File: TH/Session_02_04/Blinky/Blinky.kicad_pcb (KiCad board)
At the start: 2 copper layers, 38.1 x 38.1 mm, 12 parts, among them U1 TLC551CD‎

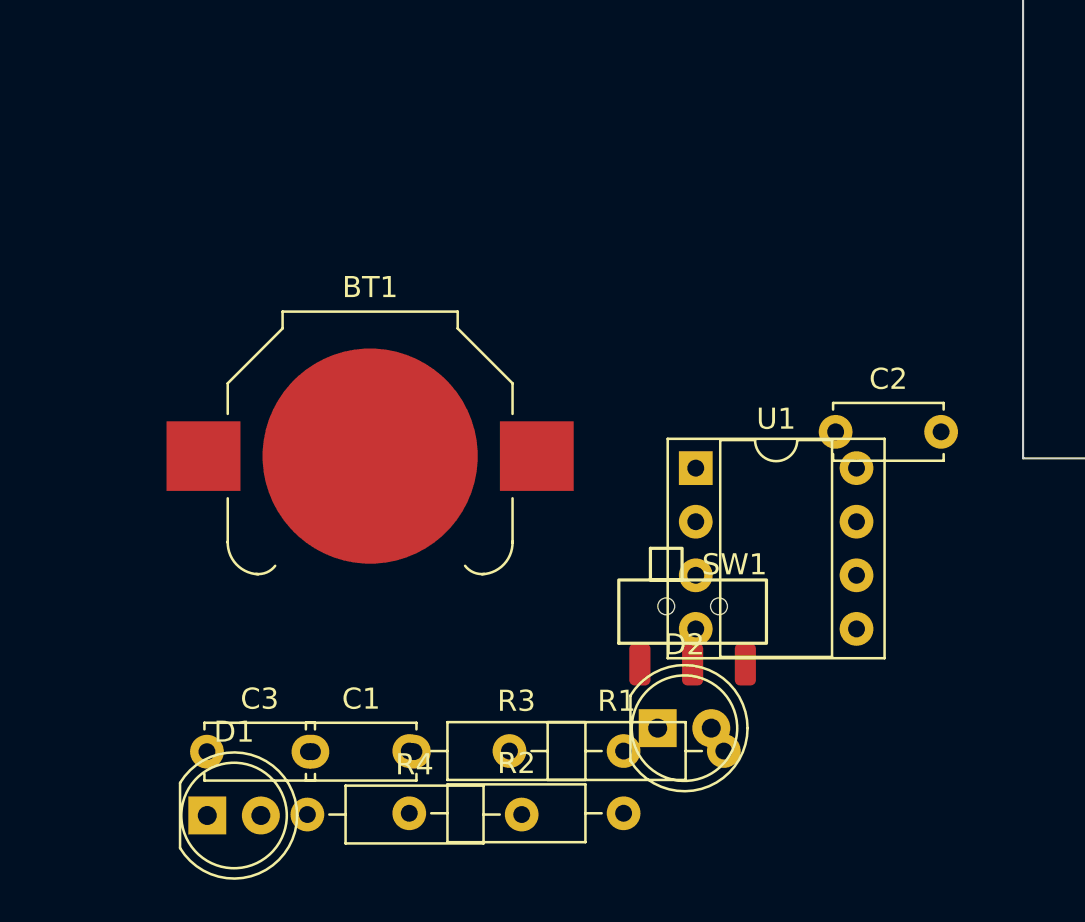
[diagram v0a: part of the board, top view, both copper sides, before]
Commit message: Revamps the through-hole project as transistor based
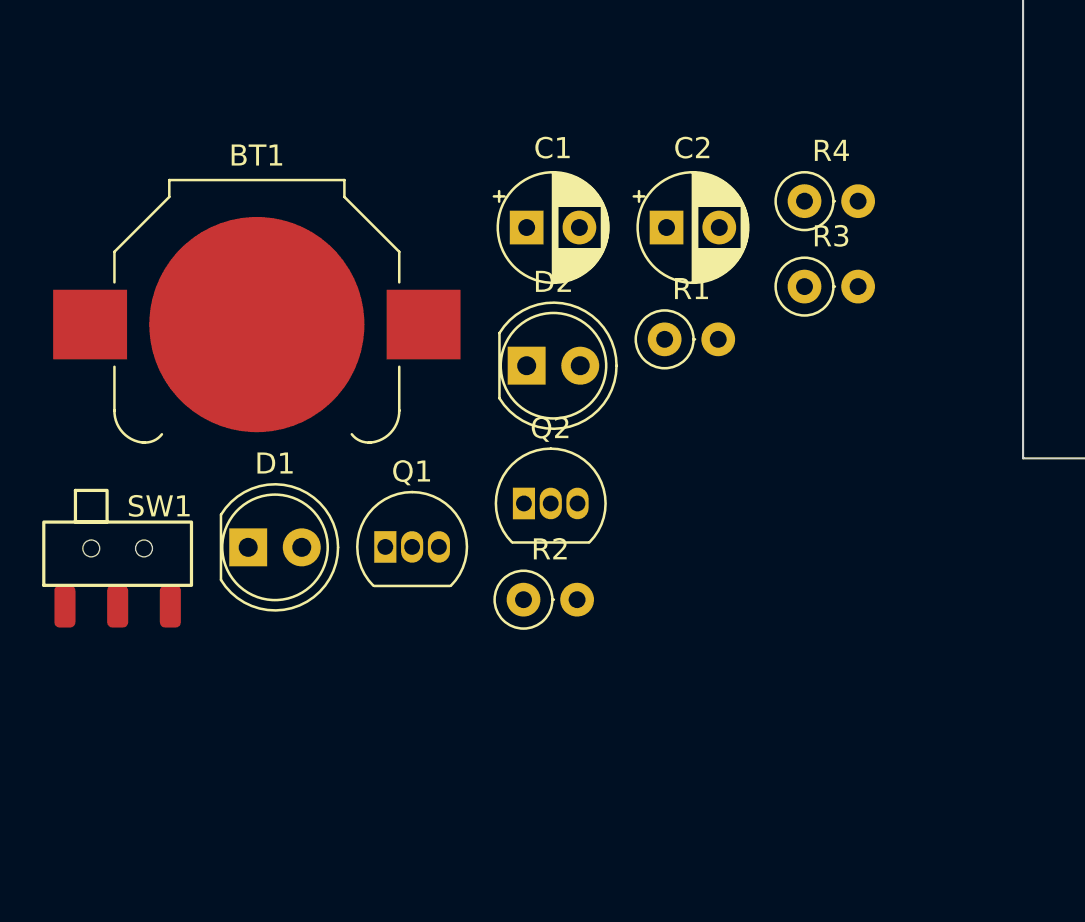
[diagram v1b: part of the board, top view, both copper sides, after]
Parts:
- removed C3: 100nF, Capacitor_THT:C_Disc_D5.0mm_W2.5mm_P5.00mm
- removed SW?: SW_SPDT, Blinky_ZAM:SSK-1202
- removed U1: TLC551CD‎, Package_DIP:DIP-8_W7.62mm_Socket
- added Q1: 2N3904, Package_TO_SOT_THT:TO-92_Inline, F.Cu at (142.0, 95.0)
- added Q2: 2N3904, Package_TO_SOT_THT:TO-92_Inline, F.Cu at (148.5, 92.9)
- added SW1: SW_SPST, Blinky_ZAM:SSK-1202, F.Cu at (129.3, 97.8)
- C1: value 300nF -> 10μF; footprint Capacitor_THT:C_Disc_D5.0mm_W2.5mm_P5.00mm -> Capacitor_THT:CP_Radial_D5.0mm_P2.50mm
- C2: value 100nF -> 10μF; footprint Capacitor_THT:C_Disc_D5.0mm_W2.5mm_P5.00mm -> Capacitor_THT:CP_Radial_D5.0mm_P2.50mm
- R1: value 10kΩ -> 220Ω; footprint Resistor_THT:R_Axial_DIN0207_L6.3mm_D2.5mm_P10.16mm_Horizontal -> Resistor_THT:R_Axial_DIN0207_L6.3mm_D2.5mm_P2.54mm_Vertical
- R2: value 1MΩ -> 100kΩ; footprint Resistor_THT:R_Axial_DIN0207_L6.3mm_D2.5mm_P10.16mm_Horizontal -> Resistor_THT:R_Axial_DIN0207_L6.3mm_D2.5mm_P2.54mm_Vertical
- R3: value 200Ω -> 100kΩ; footprint Resistor_THT:R_Axial_DIN0207_L6.3mm_D2.5mm_P10.16mm_Horizontal -> Resistor_THT:R_Axial_DIN0207_L6.3mm_D2.5mm_P2.54mm_Vertical
- R4: value 200Ω -> 220Ω; footprint Resistor_THT:R_Axial_DIN0207_L6.3mm_D2.5mm_P10.16mm_Horizontal -> Resistor_THT:R_Axial_DIN0207_L6.3mm_D2.5mm_P2.54mm_Vertical
- moved R4 37.4 mm to (161.8, 78.6)
- moved R3 28.9 mm to (161.8, 82.6)
- moved C1 26.9 mm to (148.7, 79.8)
- moved R1 20.9 mm to (155.2, 85.1)
- moved D2 18.3 mm to (148.7, 86.4)
- moved D1 12.9 mm to (135.5, 95.0)
- moved C2 12.6 mm to (155.3, 79.8)
- moved R2 11.5 mm to (148.5, 97.5)
- moved BT1 8.23 mm to (135.9, 84.4)
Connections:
- C1 pad 2: GND -> Net-(C1-Pad2)
- C2 pad 2: GND -> Net-(C2-Pad2)
- D1 pad 1: Net-(D1-Pad1) -> Net-(C1-Pad2)
- D1 pad 2: Net-(C2-Pad1) -> Net-(D1-Pad2)
- D2 pad 1: Net-(D2-Pad1) -> Net-(C2-Pad2)
- R1 pad 1: Net-(C2-Pad1) -> Net-(R1-Pad1)
- R1 pad 2: Net-(R1-Pad2) -> Net-(D1-Pad2)
- R2 pad 1: Net-(R1-Pad2) -> Net-(R1-Pad1)
- R3 pad 1: Net-(D1-Pad1) -> Net-(R1-Pad1)
- R3 pad 2: Net-(D2-Pad2) -> Net-(C2-Pad1)
- R4 pad 1: Net-(D2-Pad1) -> Net-(R1-Pad1)
- R4 pad 2: GND -> Net-(D2-Pad2)

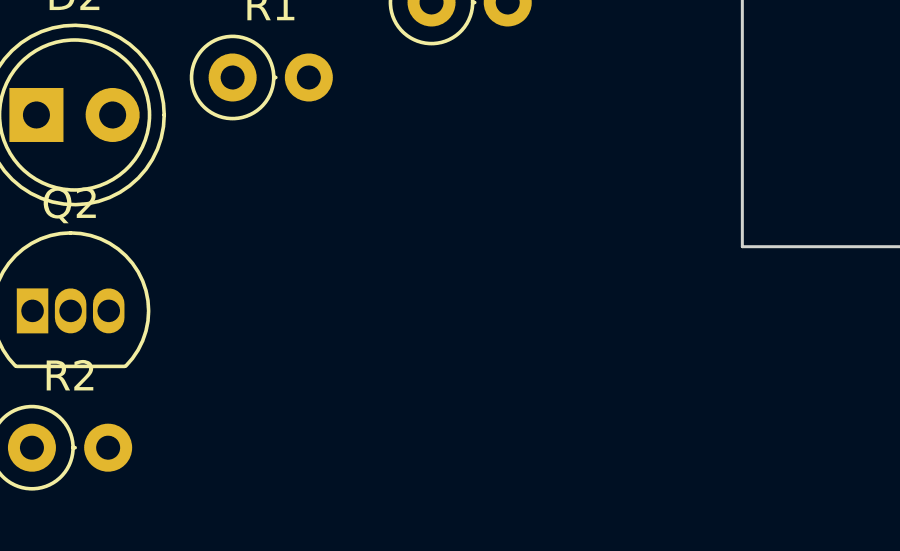
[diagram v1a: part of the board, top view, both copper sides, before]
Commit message: Makes corrections to the design rules
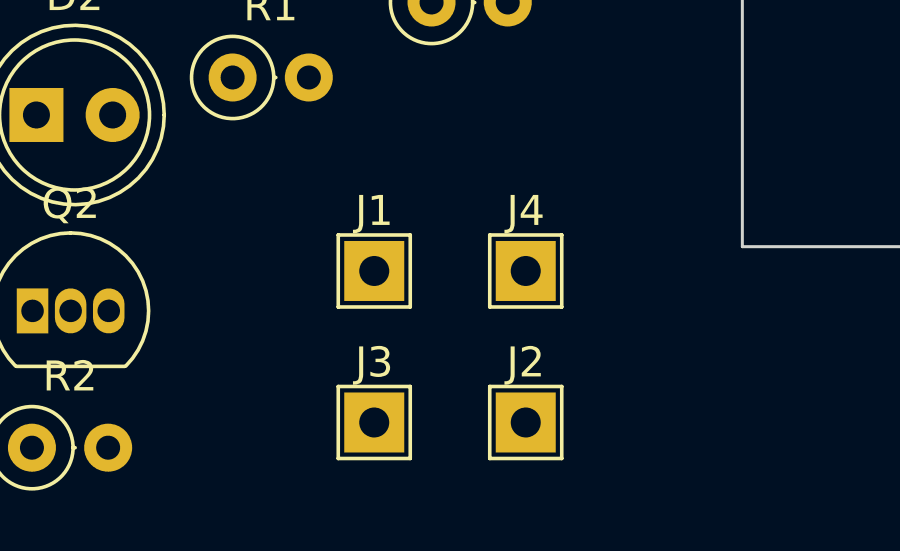
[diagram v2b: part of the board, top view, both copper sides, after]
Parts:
- added J1: Jumper_1, TestPoint:TestPoint_THTPad_2.0x2.0mm_Drill1.0mm, F.Cu at (159.9, 91.6)
- added J2: Jumper_1, TestPoint:TestPoint_THTPad_2.0x2.0mm_Drill1.0mm, F.Cu at (165.0, 96.6)
- added J4: Jumper_1, TestPoint:TestPoint_THTPad_2.0x2.0mm_Drill1.0mm, F.Cu at (165.0, 91.6)
- added J?: Jumper_1, TestPoint:TestPoint_THTPad_2.0x2.0mm_Drill1.0mm, F.Cu at (159.9, 96.6)
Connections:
- Q1 pad 2: Net-(C2-Pad1) -> Net-(J1-Pad1)
- Q2 pad 2: Net-(C1-Pad1) -> Net-(J4-Pad1)
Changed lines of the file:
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@@
     (48 "B.Fab" user)
     (49 "F.Fab" user)
-    (50 "User.1" user)
-    (51 "User.2" user)
-    (52 "User.3" user)
-    (53 "User.4" user)
-    (54 "User.5" user)
-    (55 "User.6" user)
-    (56 "User.7" user)
-    (57 "User.8" user)
-    (58 "User.9" user)
+    (50 "User.1" user "Nutzer.1")
+    (51 "User.2" user "Nutzer.2")
+    (52 "User.3" user "Nutzer.3")
+    (53 "User.4" user "Nutzer.4")
+    (54 "User.5" user "Nutzer.5")
+    (55 "User.6" user "Nutzer.6")
+    (56 "User.7" user "Nutzer.7")
+    (57 "User.8" user "Nutzer.8")
+    (58 "User.9" user "Nutzer.9")
   )
   (setup
@@
   (net 8 "Net-(D2-Pad2)")
   (net 9 "Net-(R1-Pad1)")
+  (net 10 "Net-(J1-Pad1)")
+  (net 11 "Net-(J4-Pad1)")
   (footprint "LED_THT:LED_D5.0mm" (layer "F.Cu")
     (at 135.459775 94.98)
@@
     )
   )
+  (footprint "TestPoint:TestPoint_THTPad_2.0x2.0mm_Drill1.0mm" (layer "F.Cu")
+    (at 159.92 96.62)
+    (descr "THT rectangular pad as test Point, square 2.0mm_Drill1.0mm  side length, hole diameter 1.0mm")
+    (tags "test point THT pad rectangle square")
+    (property "Reference" "J?")
+    (property "Sheetfile" "Blinky.kicad_sch")
+    (property "Sheetname" "")
+    (property "Value" "Jumper_1")
+    (attr exclude_from_pos_files)
+    (fp_text reference "J3" (at 0 -1.998) (layer "F.SilkS")
+      (effects (font (size 1 1) (thickness 0.15)))
+    )
+    (fp_text value "Jumper_1" (at 0 2.05) (layer "F.Fab")
+      (effects (font (size 1 1) (thickness 0.15)))
+    )
+    (fp_text user "${REFERENCE}" (at 0 -2) (layer "F.Fab")
+      (effects (font (size 1 1) (thickness 0.15)))
+    )
+    (fp_line (start 1.2 1.2) (end -1.2 1.2) (layer "F.SilkS") (width 0.12))
+    (fp_line (start -1.2 -1.2) (end 1.2 -1.2) (layer "F.SilkS") (width 0.12))
+    (fp_line (start 1.2 -1.2) (end 1.2 1.2) (layer "F.SilkS") (width 0.12))
+    (fp_line (start -1.2 1.2) (end -1.2 -1.2) (layer "F.SilkS") (width 0.12))
+    (fp_line (start 1.5 1.5) (end 1.5 -1.5) (layer "F.CrtYd") (width 0.05))
+    (fp_line (start -1.5 -1.5) (end -1.5 1.5) (layer "F.CrtYd") (width 0.05))
+    (fp_line (start -1.5 -1.5) (end 1.5 -1.5) (layer "F.CrtYd") (width 0.05))
+    (fp_line (start 1.5 1.5) (end -1.5 1.5) (layer "F.CrtYd") (width 0.05))
+    (pad "1" thru_hole rect (at 0 0) (size 2 2) (drill 1) (layers *.Cu *.Mask)
+      (net 4 "Net-(C2-Pad1)") (pintype "unspecified"))
+  )
   (footprint "Package_TO_SOT_THT:TO-92_Inline" (layer "F.Cu")
     (at 141.96 94.96)
@@
       (net 2 "GND") (pinfunction "E") (pintype "passive"))
     (pad "2" thru_hole oval (at 1.27 0) (size 1.05 1.5) (drill 0.75) (layers *.Cu *.Mask)
-      (net 4 "Net-(C2-Pad1)") (pinfunction "B") (pintype "passive"))
+      (net 10 "Net-(J1-Pad1)") (pinfunction "B") (pintype "passive"))
     (pad "3" thru_hole oval (at 2.54 0) (size 1.05 1.5) (drill 0.75) (layers *.Cu *.Mask)
       (net 5 "Net-(C1-Pad2)") (pinfunction "C") (pintype "passive"))
@@
       (net 2 "GND") (pinfunction "E") (pintype "passive"))
     (pad "2" thru_hole oval (at 1.27 0) (size 1.05 1.5) (drill 0.75) (layers *.Cu *.Mask)
-      (net 3 "Net-(C1-Pad1)") (pinfunction "B") (pintype "passive"))
+      (net 11 "Net-(J4-Pad1)") (pinfunction "B") (pintype "passive"))
     (pad "3" thru_hole oval (at 2.54 0) (size 1.05 1.5) (drill 0.75) (layers *.Cu *.Mask)
       (net 6 "Net-(C2-Pad2)") (pinfunction "C") (pintype "passive"))
@@
       (rotate (xyz 0 0 0))
     )
+  )
+  (footprint "TestPoint:TestPoint_THTPad_2.0x2.0mm_Drill1.0mm" (layer "F.Cu")
+    (at 164.97 91.57)
+    (descr "THT rectangular pad as test Point, square 2.0mm_Drill1.0mm  side length, hole diameter 1.0mm")
+    (tags "test point THT pad rectangle square")
+    (property "Sheetfile" "Blinky.kicad_sch")
+    (property "Sheetname" "")
+    (attr exclude_from_pos_files)
+    (fp_text reference "J4" (at 0 -1.998) (layer "F.SilkS")
+      (effects (font (size 1 1) (thickness 0.15)))
+    )
+    (fp_text value "Jumper_1" (at 0 2.05) (layer "F.Fab")
+      (effects (font (size 1 1) (thickness 0.15)))
+    )
+    (fp_text user "${REFERENCE}" (at 0 -2) (layer "F.Fab")
+      (effects (font (size 1 1) (thickness 0.15)))
+    )
+    (fp_line (start 1.2 -1.2) (end 1.2 1.2) (layer "F.SilkS") (width 0.12))
+    (fp_line (start -1.2 1.2) (end -1.2 -1.2) (layer "F.SilkS") (width 0.12))
+    (fp_line (start -1.2 -1.2) (end 1.2 -1.2) (layer "F.SilkS") (width 0.12))
+    (fp_line (start 1.2 1.2) (end -1.2 1.2) (layer "F.SilkS") (width 0.12))
+    (fp_line (start 1.5 1.5) (end -1.5 1.5) (layer "F.CrtYd") (width 0.05))
+    (fp_line (start -1.5 -1.5) (end -1.5 1.5) (layer "F.CrtYd") (width 0.05))
+    (fp_line (start -1.5 -1.5) (end 1.5 -1.5) (layer "F.CrtYd") (width 0.05))
+    (fp_line (start 1.5 1.5) (end 1.5 -1.5) (layer "F.CrtYd") (width 0.05))
+    (pad "1" thru_hole rect (at 0 0) (size 2 2) (drill 1) (layers *.Cu *.Mask)
+      (net 11 "Net-(J4-Pad1)") (pintype "unspecified"))
   )
   (footprint "Resistor_THT:R_Axial_DIN0207_L6.3mm_D2.5mm_P2.54mm_Vertical" (layer "F.Cu")
@@
     )
   )
+  (footprint "TestPoint:TestPoint_THTPad_2.0x2.0mm_Drill1.0mm" (layer "F.Cu")
+    (at 164.97 96.62)
+    (descr "THT rectangular pad as test Point, square 2.0mm_Drill1.0mm  side length, hole diameter 1.0mm")
+    (tags "test point THT pad rectangle square")
+    (property "Sheetfile" "Blinky.kicad_sch")
+    (property "Sheetname" "")
+    (attr exclude_from_pos_files)
+    (fp_text reference "J2" (at 0 -1.998) (layer "F.SilkS")
+      (effects (font (size 1 1) (thickness 0.15)))
+    )
+    (fp_text value "Jumper_1" (at 0 2.05) (layer "F.Fab")
+      (effects (font (size 1 1) (thickness 0.15)))
+    )
+    (fp_text user "${REFERENCE}" (at 0 -2) (layer "F.Fab")
+      (effects (font (size 1 1) (thickness 0.15)))
+    )
+    (fp_line (start -1.2 -1.2) (end 1.2 -1.2) (layer "F.SilkS") (width 0.12))
+    (fp_line (start -1.2 1.2) (end -1.2 -1.2) (layer "F.SilkS") (width 0.12))
+    (fp_line (start 1.2 1.2) (end -1.2 1.2) (layer "F.SilkS") (width 0.12))
+    (fp_line (start 1.2 -1.2) (end 1.2 1.2) (layer "F.SilkS") (width 0.12))
+    (fp_line (start 1.5 1.5) (end 1.5 -1.5) (layer "F.CrtYd") (width 0.05))
+    (fp_line (start 1.5 1.5) (end -1.5 1.5) (layer "F.CrtYd") (width 0.05))
+    (fp_line (start -1.5 -1.5) (end 1.5 -1.5) (layer "F.CrtYd") (width 0.05))
+    (fp_line (start -1.5 -1.5) (end -1.5 1.5) (layer "F.CrtYd") (width 0.05))
+    (pad "1" thru_hole rect (at 0 0) (size 2 2) (drill 1) (layers *.Cu *.Mask)
+      (net 3 "Net-(C1-Pad1)") (pintype "unspecified"))
+  )
   (footprint "Blinky_ZAM:SSK-1202" (layer "F.Cu")
     (at 129.271201 97.781199)
@@
     (pad "3" smd roundrect (at 2.5 0) (size 1 2) (layers "F.Cu" "F.Paste" "F.Mask") (roundrect_rratio 0.25))
   )
+  (footprint "TestPoint:TestPoint_THTPad_2.0x2.0mm_Drill1.0mm" (layer "F.Cu")
+    (at 159.92 91.57)
+    (descr "THT rectangular pad as test Point, square 2.0mm_Drill1.0mm  side length, hole diameter 1.0mm")
+    (tags "test point THT pad rectangle square")
+    (property "Sheetfile" "Blinky.kicad_sch")
+    (property "Sheetname" "")
+    (attr exclude_from_pos_files)
+    (fp_text reference "J1" (at 0 -1.998) (layer "F.SilkS")
+      (effects (font (size 1 1) (thickness 0.15)))
+    )
+    (fp_text value "Jumper_1" (at 0 2.05) (layer "F.Fab")
+      (effects (font (size 1 1) (thickness 0.15)))
+    )
+    (fp_text user "${REFERENCE}" (at 0 -2) (layer "F.Fab")
+      (effects (font (size 1 1) (thickness 0.15)))
+    )
+    (fp_line (start -1.2 1.2) (end -1.2 -1.2) (layer "F.SilkS") (width 0.12))
+    (fp_line (start 1.2 -1.2) (end 1.2 1.2) (layer "F.SilkS") (width 0.12))
+    (fp_line (start 1.2 1.2) (end -1.2 1.2) (layer "F.SilkS") (width 0.12))
+    (fp_line (start -1.2 -1.2) (end 1.2 -1.2) (layer "F.SilkS") (width 0.12))
+    (fp_line (start 1.5 1.5) (end -1.5 1.5) (layer "F.CrtYd") (width 0.05))
+    (fp_line (start -1.5 -1.5) (end -1.5 1.5) (layer "F.CrtYd") (width 0.05))
+    (fp_line (start 1.5 1.5) (end 1.5 -1.5) (layer "F.CrtYd") (width 0.05))
+    (fp_line (start -1.5 -1.5) (end 1.5 -1.5) (layer "F.CrtYd") (width 0.05))
+    (pad "1" thru_hole rect (at 0 0) (size 2 2) (drill 1) (layers *.Cu *.Mask)
+      (net 10 "Net-(J1-Pad1)") (pintype "unspecified"))
+  )
   (gr_rect (start 172.19 52.66) (end 210.29 90.76) (layer "Edge.Cuts") (width 0.1) (fill none))

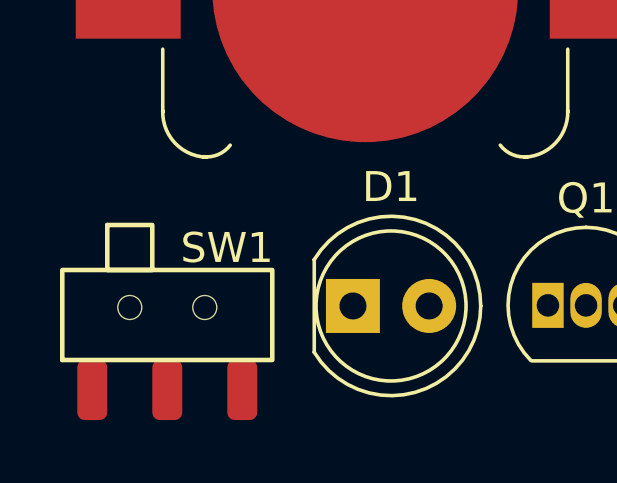
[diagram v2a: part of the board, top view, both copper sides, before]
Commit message: Corrections to the switch footprint
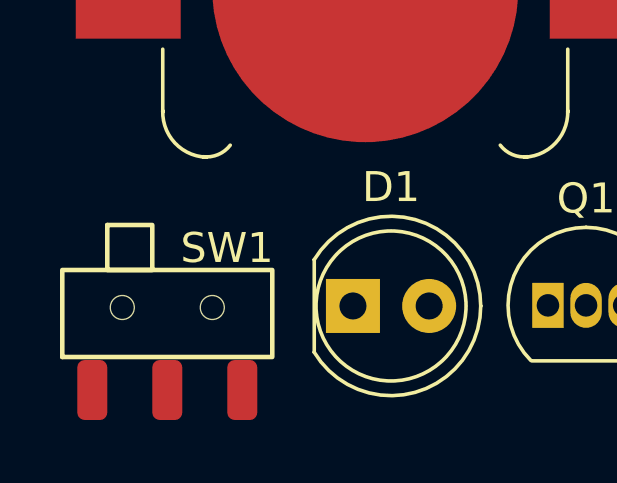
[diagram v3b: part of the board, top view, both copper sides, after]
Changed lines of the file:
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@@
       (effects (font (size 1 1) (thickness 0.15)))
     )
+    (fp_rect (start -3.500001 -1.1) (end 3.500001 -4) (layer "F.SilkS") (width 0.1524) (fill none))
     (fp_rect (start -2 -5.499999) (end -0.5 -4) (layer "F.SilkS") (width 0.1524) (fill none))
-    (fp_rect (start -3.500001 -1) (end 3.500001 -4) (layer "F.SilkS") (width 0.1524) (fill none))
     (fp_rect (start -3.5 -5.5) (end 3.5 1) (layer "F.CrtYd") (width 0.01) (fill none))
-    (pad "" np_thru_hole circle (at -1.25 -2.75) (size 0.8 0.8) (drill 0.8) (layers F&B.Cu *.Mask))
-    (pad "" np_thru_hole circle (at 1.25 -2.75) (size 0.8 0.8) (drill 0.8) (layers F&B.Cu *.Mask))
+    (pad "" np_thru_hole circle (at 1.5 -2.75) (size 0.8 0.8) (drill 0.8) (layers F&B.Cu *.Mask))
+    (pad "" np_thru_hole circle (at -1.5 -2.75) (size 0.8 0.8) (drill 0.8) (layers F&B.Cu *.Mask))
     (pad "1" smd roundrect (at -2.5 0) (size 1 2) (layers "F.Cu" "F.Paste" "F.Mask") (roundrect_rratio 0.25)
       (net 1 "Net-(BT1-Pad1)") (pinfunction "A") (pintype "passive"))
